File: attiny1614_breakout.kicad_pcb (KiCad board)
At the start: 2 copper layers, 15.2 x 20.3 mm, 15 parts, among them J1 Conn_01x07, J2 Conn_01x07, J3 UPDI, SW1 Reset, U1 REG102-5, U2 ATtiny1614-SS

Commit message: fixed solder mask clearance
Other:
- net class Default: trace_width 0.1524 -> 0.254; via_dia 0.6096 -> 0.508; via_drill 0.3048 -> 0.254
- rule pad_to_mask_clearance: 0.051 -> 0.0508
- rule via_min_drill: 0.2286 -> 0.254
- rule via_min_size: 0.4572 -> 0.508
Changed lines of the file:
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@@
   )
   (setup
-    (last_trace_width 0.1524)
+    (last_trace_width 0.254)
     (user_trace_width 0.254)
-    (user_trace_width 0.3048)
     (trace_clearance 0.1524)
     (zone_clearance 0.1524)
     (zone_45_only no)
     (trace_min 0.1524)
-    (via_size 0.6096)
-    (via_drill 0.3048)
-    (via_min_size 0.4572)
-    (via_min_drill 0.2286)
-    (user_via 0.4572 0.2286)
+    (via_size 0.508)
+    (via_drill 0.254)
+    (via_min_size 0.508)
+    (via_min_drill 0.254)
     (user_via 0.508 0.254)
     (uvia_size 0.3)
@@
     (pad_size 1.524 1.524)
     (pad_drill 0.762)
-    (pad_to_mask_clearance 0.051)
-    (solder_mask_min_width 0.25)
+    (pad_to_mask_clearance 0.0508)
     (aux_axis_origin 0 0)
     (visible_elements FFFFFF7F)
@@
   (net_class Default "This is the default net class."
     (clearance 0.1524)
-    (trace_width 0.1524)
-    (via_dia 0.6096)
-    (via_drill 0.3048)
+    (trace_width 0.254)
+    (via_dia 0.508)
+    (via_drill 0.254)
     (uvia_dia 0.3)
     (uvia_drill 0.1)

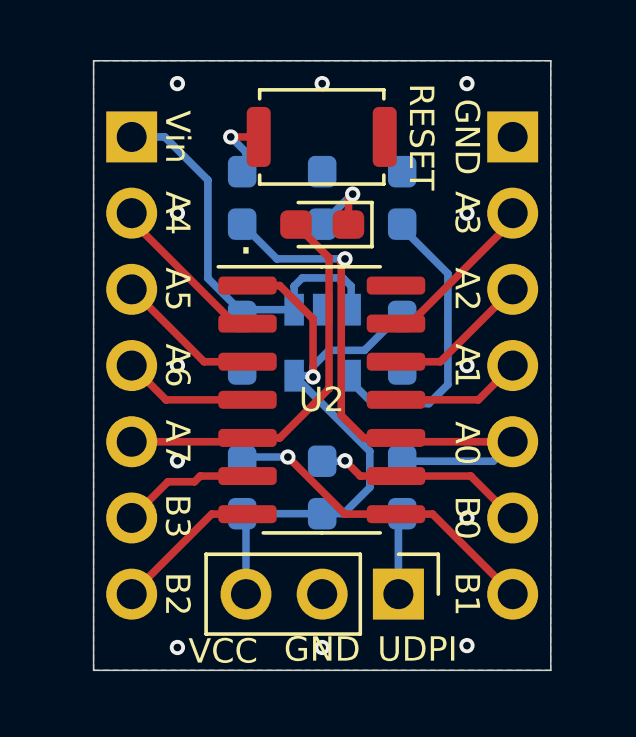
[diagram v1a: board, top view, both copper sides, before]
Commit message: moved to programmer pin to Vin, fixed typos, added thermal relief
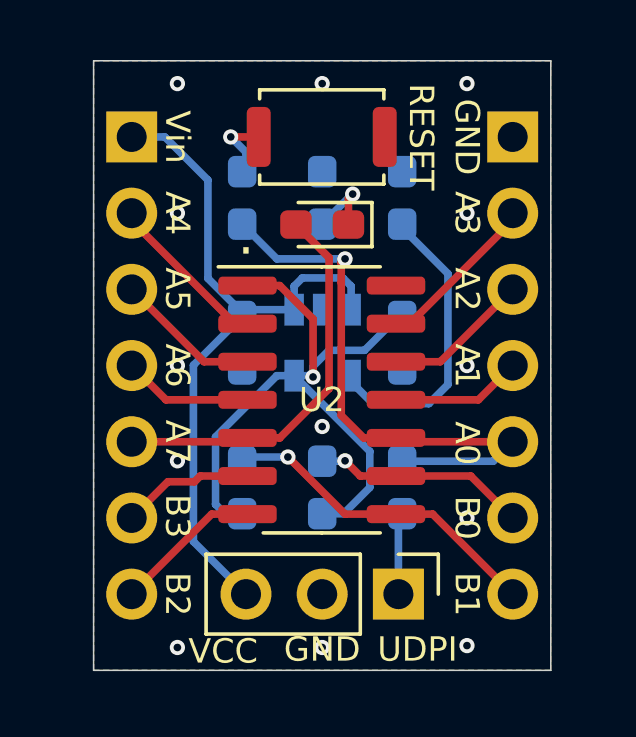
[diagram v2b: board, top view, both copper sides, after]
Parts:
- C1: value 100nF -> 1uF
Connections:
- J3 pad 3: VCC -> /V_in
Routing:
- net /V_in: track 13.6 -> 24.1 mm
- net VCC: track 21.1 -> 22.6 mm
- net GND: vias 12 -> 13
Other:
- board text added: "ATtiny1614 Breakout v1.2"
- board text removed: "ATtiny1614 Breakout v1.0"
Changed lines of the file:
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@@
     (thickness 1.6)
     (drawings 25)
-    (tracks 110)
+    (tracks 118)
     (zones 0)
     (modules 15)
@@
     (34 B.Paste user hide)
     (35 F.Paste user hide)
-    (36 B.SilkS user)
-    (37 F.SilkS user)
+    (36 B.SilkS user hide)
+    (37 F.SilkS user hide)
     (38 B.Mask user hide)
     (39 F.Mask user hide)
@@
     (44 Edge.Cuts user)
     (45 Margin user hide)
-    (46 B.CrtYd user)
+    (46 B.CrtYd user hide)
     (47 F.CrtYd user hide)
     (48 B.Fab user hide)
@@
     (fp_line (start -0.635 -1.27) (end 1.27 -1.27) (layer F.Fab) (width 0.1))
     (pad 3 thru_hole oval (at 0 5.08 270) (size 1.7 1.7) (drill 1) (layers *.Cu *.Mask)
-      (net 3 VCC))
+      (net 2 /V_in))
     (pad 2 thru_hole oval (at 0 2.54 270) (size 1.7 1.7) (drill 1) (layers *.Cu *.Mask)
       (net 1 GND))
@@
       (effects (font (size 0.8128 0.8128) (thickness 0.1524)) (justify mirror))
     )
-    (fp_text value 100nF (at 0 -1.43 90) (layer B.Fab)
+    (fp_text value 1uF (at 0 -1.43 90) (layer B.Fab)
       (effects (font (size 1 1) (thickness 0.15)) (justify mirror))
     )
@@
     (effects (font (size 0.8128 0.8128) (thickness 0.1524)))
   )
-  (gr_text "ATtiny1614 Breakout v1.0" (at 124.079 88.9 90) (layer B.SilkS)
+  (gr_text "ATtiny1614 Breakout v1.2" (at 124.079 88.9 90) (layer B.SilkS)
     (effects (font (size 0.8128 0.8128) (thickness 0.1524)) (justify mirror))
   )
@@
   (via (at 123.444 83.82) (size 0.508) (drill 0.254) (layers F.Cu B.Cu) (net 1))
   (via (at 133.096 83.82) (size 0.508) (drill 0.254) (layers F.Cu B.Cu) (net 1))
+  (via (at 128.27 90.932) (size 0.508) (drill 0.254) (layers F.Cu B.Cu) (net 1))
   (segment (start 129.235 86.254) (end 129.235 87.038) (width 0.254) (layer B.Cu) (net 2))
   (segment (start 128.96 85.979) (end 129.235 86.254) (width 0.254) (layer B.Cu) (net 2))
@@
   (segment (start 124.46 82.716) (end 124.46 85.993) (width 0.254) (layer B.Cu) (net 2))
   (segment (start 123.024 81.28) (end 124.46 82.716) (width 0.254) (layer B.Cu) (net 2))
-  (segment (start 125.73 96.52) (end 125.73 93.839) (width 0.254) (layer B.Cu) (net 3) (status 30))
-  (segment (start 128.27 93.839) (end 125.73 93.839) (width 0.254) (layer B.Cu) (net 3) (status 30))
+  (segment (start 123.977401 94.767401) (end 125.32359 96.11359) (width 0.254) (layer B.Cu) (net 2))
+  (segment (start 125.32359 96.11359) (end 125.32359 96.52) (width 0.254) (layer B.Cu) (net 2))
+  (segment (start 123.977401 88.888599) (end 123.977401 94.767401) (width 0.254) (layer B.Cu) (net 2))
+  (segment (start 125.603 87.263) (end 123.977401 88.888599) (width 0.254) (layer B.Cu) (net 2))
   (segment (start 129.681 88.392) (end 128.494961 88.392) (width 0.254) (layer B.Cu) (net 3))
   (segment (start 126.855 86.233) (end 127.965179 87.343179) (width 0.254) (layer F.Cu) (net 3))
@@
   (segment (start 129.8575 92.964) (end 129.8575 91.7575) (width 0.254) (layer B.Cu) (net 3))
   (segment (start 128.27 93.839) (end 128.9825 93.839) (width 0.254) (layer B.Cu) (net 3))
+  (segment (start 124.714 91.28) (end 126.756 89.238) (width 0.254) (layer B.Cu) (net 3))
+  (segment (start 124.714 93.525) (end 124.714 91.28) (width 0.254) (layer B.Cu) (net 3))
+  (segment (start 125.028 93.839) (end 124.714 93.525) (width 0.254) (layer B.Cu) (net 3))
+  (segment (start 126.756 89.238) (end 127.335 89.238) (width 0.254) (layer B.Cu) (net 3))
+  (segment (start 125.603 93.839) (end 125.028 93.839) (width 0.254) (layer B.Cu) (net 3))
   (segment (start 125.653 91.44) (end 125.78 91.313) (width 0.254) (layer F.Cu) (net 4) (status 30))
   (segment (start 121.92 91.44) (end 125.653 91.44) (width 0.254) (layer F.Cu) (net 4) (status 30))
@@
   (segment (start 125.222 81.28) (end 126.155 81.28) (width 0.254) (layer F.Cu) (net 19) (status 20))
   (zone (net 1) (net_name GND) (layer B.Cu) (hatch edge 0.508)
-    (connect_pads thru_hole_only (clearance 0.1524))
+    (connect_pads (clearance 0.1524))
     (min_thickness 0.1524)
     (fill yes (arc_segments 32) (thermal_gap 0.254) (thermal_bridge_width 0.254))
@@
   )
   (zone (net 1) (net_name GND) (layer F.Cu) (hatch edge 0.508)
-    (connect_pads thru_hole_only (clearance 0.1524))
+    (connect_pads (clearance 0.1524))
     (min_thickness 0.1524)
     (fill yes (arc_segments 32) (thermal_gap 0.254) (thermal_bridge_width 0.254))

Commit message: Fixed silkscreen typos
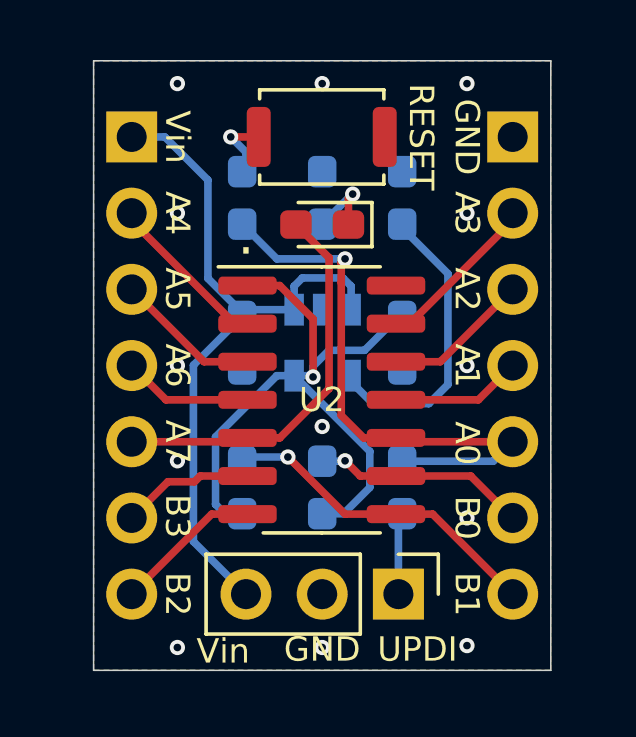
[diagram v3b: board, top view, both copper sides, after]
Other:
- board text added: "UPDI"
- board text removed: "UDPI"
- board text removed: "VCC"
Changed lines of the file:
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@@
   )
   (layers
-    (0 F.Cu signal)
-    (31 B.Cu signal)
+    (0 F.Cu signal hide)
+    (31 B.Cu signal hide)
     (32 B.Adhes user hide)
     (33 F.Adhes user hide)
@@
     (35 F.Paste user hide)
     (36 B.SilkS user hide)
-    (37 F.SilkS user hide)
+    (37 F.SilkS user)
     (38 B.Mask user hide)
     (39 F.Mask user hide)
@@
     (effects (font (size 1.27 1.27) (thickness 0.254)))
   )
-  (gr_text VCC (at 124.968 98.425) (layer F.SilkS)
+  (gr_text Vin (at 124.968 98.425) (layer F.SilkS)
     (effects (font (size 0.8128 0.8128) (thickness 0.1524)))
   )
@@
     (effects (font (size 0.8128 0.8128) (thickness 0.1524)))
   )
-  (gr_text UDPI (at 131.445 98.3615) (layer F.SilkS)
+  (gr_text UPDI (at 131.445 98.3615) (layer F.SilkS)
     (effects (font (size 0.8128 0.8128) (thickness 0.1524)))
   )

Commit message: additional silkscreen labels, cleaned-up gnd plane
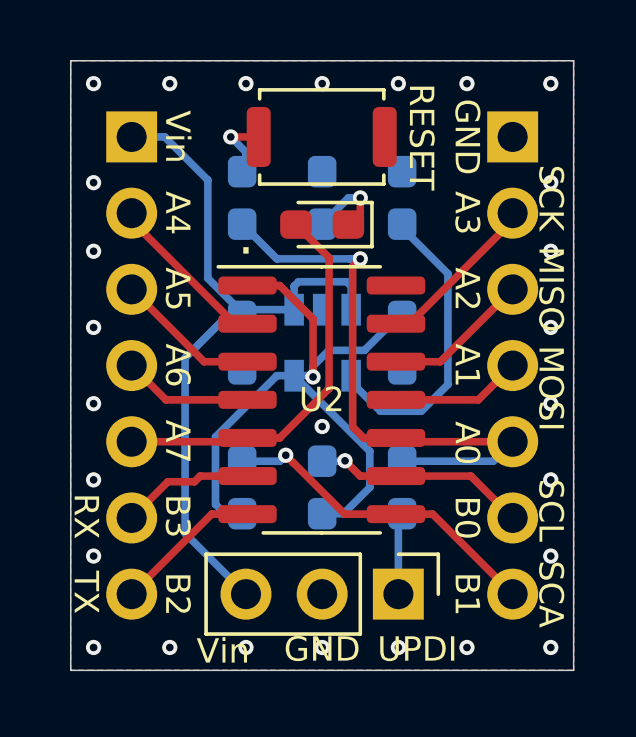
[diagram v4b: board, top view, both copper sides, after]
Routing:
- net GND: vias 13 -> 27
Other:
- board size 15.2 x 20.3 mm -> 16.8 x 20.3 mm
- board text added: "MISO"
- board text added: "MOSI"
- board text added: "RX"
- board text added: "SCA"
- board text added: "SCK"
- board text added: "SCL"
- board text added: "TX"

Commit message: changed VCC to 5V
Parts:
- U1: value REG102-5 -> LP2985
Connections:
- net VCC renamed +5V
